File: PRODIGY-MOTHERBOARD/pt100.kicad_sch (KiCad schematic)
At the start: 5 parts, among them U10 LMP2011, U11 LMP2011, U17 LMP2011, U27 LMP2011, U9 LM4125AIM5-2.5

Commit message: Finished v0.1 schematic.
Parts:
- added C90: 100nF, symbol Device:C
- added C91: 47uF, symbol Device:C
- added JP10, JP9: Jumper_2_Open, symbol Jumper:Jumper_2_Open
- added R80: 2.5k, symbol Device:R
- added R81, R83, R84, R85, R86, R87: 10k, symbol Device:R
- added R82: 3.205k, symbol Device:R
- renumbered U10 to U23, U9 to U24, U11 to U25, U17 to U26
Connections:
- net at U26.1: now also R83.2, R85.1
- net GND: now reaches U26.2 (V-)
- net GND: now also U23.2 (V-), U24.2 (GND), U25.2 (V-), U27.2 (V-), C91.2, R80.2, R86.2
- net at U26.3 (+): now also R82.2, R83.1
- net RTD_W3: now reaches U26.4 (-)
- net RTD_W3: now also C90.2, JP10.1 (A)
- net +3.3VA: now reaches U26.5 (V+)
- net +3.3VA: now also U23.5 (V+), U24.4 (Vin), U25.5 (V+), U27.5 (V+)
- net RTD_A_OUT: now reaches U27.1
- net RTD_A_OUT: now also R87.2
- net at U27.3 (+): now also R84.2, R86.1
- net at U27.4 (-): now also R85.2, R87.1
- net at U24.5 (Vout): now also U23.3 (+), C91.1
- net RTD_W1: now reaches U23.1
- net RTD_W1: now also JP9.1 (A)
- net RTD_W4: now reaches U23.4 (-)
- net RTD_W4: now also JP10.2 (B), R80.1
- net at U25.1: now also R81.1, R84.1
- net RTD_W2: now reaches U25.3 (+)
- net RTD_W2: now also C90.1, JP9.2 (B)
- net at U25.4 (-): now also R81.2, R82.1
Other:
- note added: "2/3/4 Wire Configurator"
- note added: "Constant Current Source: 1mA 1mA = 2.5V / 2.5kOhm"
- note added: "Instrumentation Amplifier"
- note added: "Output voltage range: 0,1V - 0.34528V Gain: 2.5/0.34528 = 7.2405 R7 = 3.205k"
- moved on the sheet: U23, U24, U25, U26, U27

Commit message: schematic v0.2 finalized
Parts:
- renumbered C90 to C87, C91 to C88, JP9 to JP10, JP10 to JP11, R80 to R77, R81 to R78, R82 to R79, R83 to R80, R84 to R81, R85 to R82, R86 to R83, R87 to R84, U23 to U22, U24 to U23, U25 to U24, U26 to U25, U27 to U26

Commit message: Motherboard footprints assigned.
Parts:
- C87: footprint (none) -> Capacitor_SMD:C_0603_1608Metric
- C88: footprint (none) -> Capacitor_SMD:C_1210_3225Metric
- JP10, JP11: footprint (none) -> Connector_PinHeader_2.54mm:PinHeader_1x02_P2.54mm_Vertical
- R77, R78, R79, R80, R81, R82, R83, R84: footprint (none) -> Resistor_SMD:R_0603_1608Metric
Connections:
- net +3.3VA renamed VAA
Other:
- moved on the sheet: R79

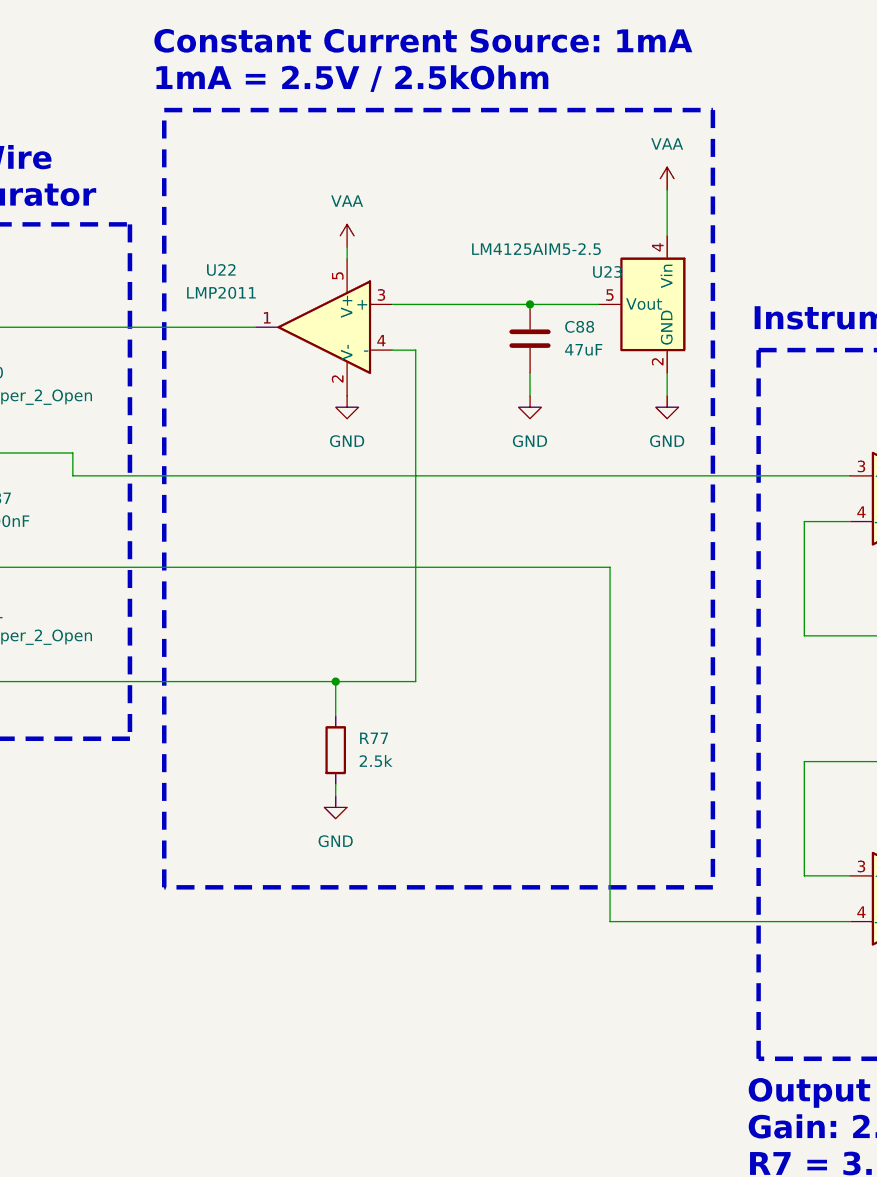
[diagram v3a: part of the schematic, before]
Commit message: finished motherboard bom and updated footprints
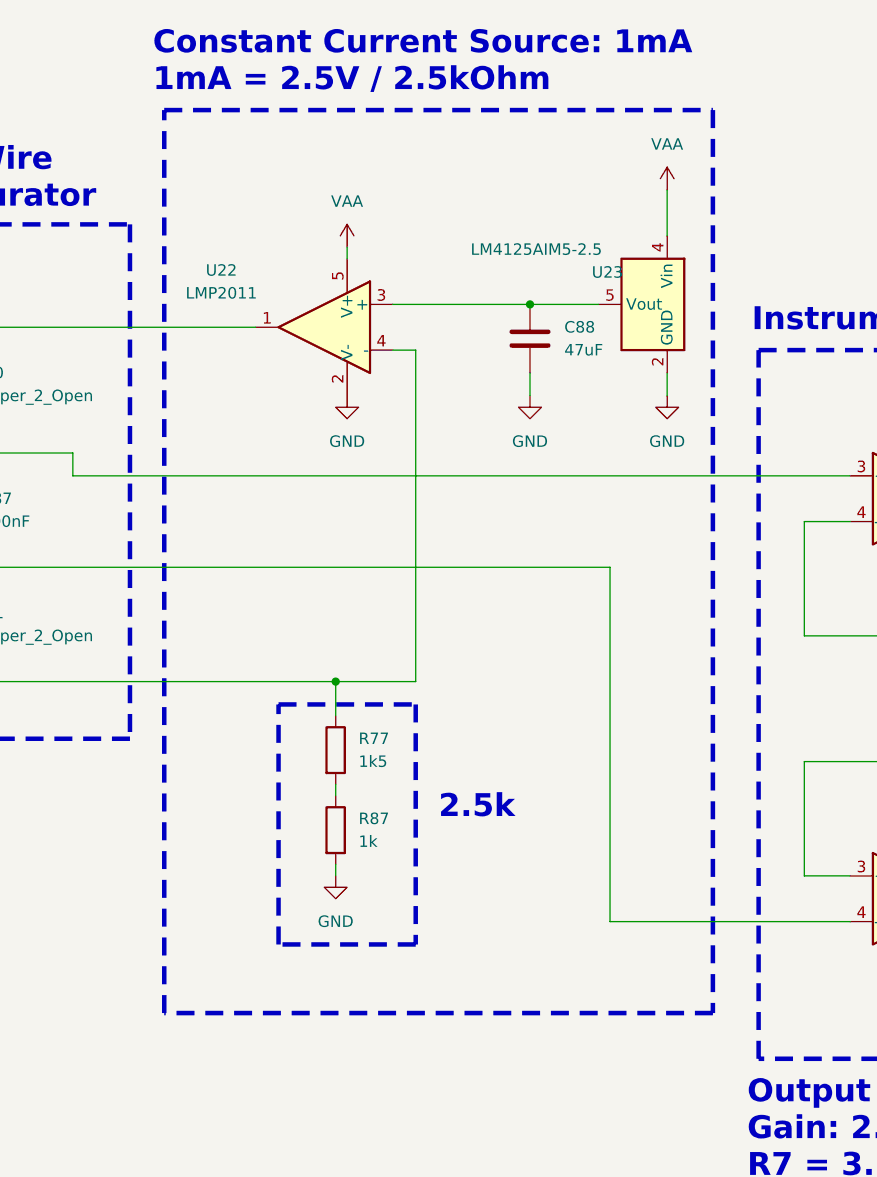
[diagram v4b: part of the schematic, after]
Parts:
- added R87: 1k, Resistor_SMD:R_0603_1608Metric, symbol Device:R
- C87: TME (none) -> CL10B104KB8NNNC
- C88: TME (none) -> GRM32ER61C476KE15L
- JP10, JP11: TME (none) -> JUMPER-H/B
- R77: value 2.5k -> 1k5; TME (none) -> WR06X1501FTL
- R78, R80, R81, R82, R83, R84: TME (none) -> WR06X1002FTL
- R79: TME (none) -> ERA3AEB332V
- U22, U24, U25, U26: MOUSER (none) -> 926-LMP2011MFX/NOPB
- U23: MOUSER (none) -> 926-LM4125IM525NOPB
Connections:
- net GND: now also R87.2; no longer R77.2
- new net: R77.2, R87.1
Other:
- note added: "2.5k"
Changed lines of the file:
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@@
 	(wire
 		(pts
-			(xy 114.3 114.3) (xy 114.3 113.03)
-		)
-		(stroke
-			(width 0)
-			(type default)
-		)
-	)
-	(wire
-		(pts
 			(xy 166.37 123.19) (xy 166.37 110.49)
 		)
@@
 	(wire
 		(pts
+			(xy 114.3 123.19) (xy 114.3 121.92)
+		)
+		(stroke
+			(width 0)
+			(type default)
+		)
+	)
+	(wire
+		(pts
 			(xy 199.39 96.52) (xy 199.39 99.06)
 		)
@@
 	(wire
 		(pts
+			(xy 114.3 113.03) (xy 114.3 114.3)
+		)
+		(stroke
+			(width 0)
+			(type default)
+		)
+	)
+	(wire
+		(pts
 			(xy 218.44 104.14) (xy 215.9 104.14)
 		)
@@
 	(rectangle
 		(start 95.25 38.1)
-		(end 156.21 124.46)
+		(end 156.21 138.43)
+		(stroke
+			(width 0.5)
+			(type dash)
+		)
+		(fill
+			(type none)
+		)
+	)
+	(rectangle
+		(start 107.95 104.14)
+		(end 123.19 130.81)
 		(stroke
 			(width 0.5)
@@
 		)
 	)
+	(text "2.5k"
+		(exclude_from_sim no)
+		(at 125.73 117.094 0)
+		(effects
+			(font
+				(size 2.54 2.54)
+				(thickness 0.508)
+				(bold yes)
+			)
+			(justify left bottom)
+		)
+	)
 	(hierarchical_label "RTD_W1"
 		(shape input)
@@
 			)
 		)
-		(property "MOUSER" ""
+		(property "MOUSER" " 926-LMP2011MFX/NOPB "
 			(at 179.07 125.73 0)
 			(effects
@@
 			)
 		)
-		(property "TME" ""
+		(property "TME" "WR06X1002FTL "
 			(at 199.39 120.65 0)
 			(effects
@@
 			)
 		)
-		(property "TME" ""
+		(property "TME" "GRM32ER61C476KE15L"
 			(at 135.89 63.5 0)
 			(effects
@@
 			)
 		)
-		(property "TME" ""
+		(property "TME" "JUMPER-H/B"
 			(at 71.12 68.58 0)
 			(effects
@@
 			)
 		)
-		(property "TME" ""
+		(property "TME" "WR06X1002FTL "
 			(at 209.55 81.28 0)
 			(effects
@@
 			)
 		)
-		(property "MOUSER" ""
+		(property "MOUSER" " 926-LMP2011MFX/NOPB "
 			(at 226.06 101.6 0)
 			(effects
@@
 			)
 		)
-		(property "TME" ""
+		(property "TME" "WR06X1002FTL "
 			(at 210.82 125.73 0)
 			(effects
@@
 			)
 		)
-		(property "TME" ""
+		(property "TME" "JUMPER-H/B"
 			(at 71.12 95.25 0)
 			(effects
@@
 			)
 		)
-		(property "MOUSER" ""
+		(property "MOUSER" " 926-LM4125IM525NOPB "
 			(at 151.13 59.69 0)
 			(effects
@@
 			)
 		)
-		(property "MOUSER" ""
+		(property "MOUSER" " 926-LMP2011MFX/NOPB "
 			(at 113.03 62.23 0)
 			(effects
@@
 			)
 		)
-		(property "TME" ""
+		(property "TME" "WR06X1002FTL "
 			(at 224.79 125.73 0)
 			(effects
@@
 			)
 		)
-		(property "TME" ""
+		(property "TME" "CL10B104KB8NNNC  "
 			(at 71.12 82.55 0)
 			(effects
@@
 	)
 	(symbol
+		(lib_id "Device:R")
+		(at 114.3 118.11 0)
+		(unit 1)
+		(exclude_from_sim no)
+		(in_bom yes)
+		(on_board yes)
+		(dnp no)
+		(property "Reference" "R87"
+			(at 116.84 116.8399 0)
+			(effects
+				(font
+					(size 1.27 1.27)
+				)
+				(justify left)
+			)
+		)
+		(property "Value" "1k"
+			(at 116.84 119.3799 0)
+			(effects
+				(font
+					(size 1.27 1.27)
+				)
+				(justify left)
+			)
+		)
+		(property "Footprint" "Resistor_SMD:R_0603_1608Metric"
+			(at 112.522 118.11 90)
+			(effects
+				(font
+					(size 1.27 1.27)
+				)
+				(hide yes)
+			)
+		)
+		(property "Datasheet" "~"
+			(at 114.3 118.11 0)
+			(effects
+				(font
+					(size 1.27 1.27)
+				)
+				(hide yes)
+			)
+		)
+		(property "Description" "Resistor"
+			(at 114.3 118.11 0)
+			(effects
+				(font
+					(size 1.27 1.27)
+				)
+				(hide yes)
+			)
+		)
+		(property "MOUSER" ""
+			(at 114.3 118.11 0)
+			(effects
+				(font
+					(size 1.27 1.27)
+				)
+				(hide yes)
+			)
+		)
+		(property "Sim.Type" ""
+			(at 114.3 118.11 0)
+			(effects
+				(font
+					(size 1.27 1.27)
+				)
+				(hide yes)
+			)
+		)
+		(property "TME" "RC0603JR-071K "
+			(at 114.3 118.11 0)
+			(effects
+				(font
+					(size 1.27 1.27)
+				)
+				(hide yes)
+			)
+		)
+		(pin "2"
+		)
+		(pin "1"
+		)
+		(instances
+			(project "PRODIGY-MOTHERBOARD"
+				(path "/f1c25860-8989-4190-bd24-2491d23ca7d9/1fb3a40b-5b56-4526-bac8-0d25e381d4b7"
+					(reference "R87")
+					(unit 1)
+				)
+			)
+		)
+	)
+	(symbol
 		(lib_id "power:VAA")
 		(at 176.53 72.39 0)
@@
 			)
 		)
-		(property "MOUSER" ""
+		(property "MOUSER" " 926-LMP2011MFX/NOPB "
 			(at 179.07 81.28 0)
 			(effects
@@
 			)
 		)
-		(property "Value" "2.5k"
+		(property "Value" "1k5"
 			(at 116.84 110.4899 0)
 			(effects
@@
 			)
 		)
-		(property "TME" ""
+		(property "TME" "WR06X1501FTL "
 			(at 114.3 109.22 0)
 			(effects
@@
 			)
 		)
-		(property "TME" ""
+		(property "TME" "ERA3AEB332V"
 			(at 199.39 102.87 0)
 			(effects
@@
 			)
 		)
-		(property "TME" ""
+		(property "TME" "WR06X1002FTL "
 			(at 199.39 86.36 0)
 			(effects
@@
 			)
 		)
-		(property "TME" ""
+		(property "TME" "WR06X1002FTL "
 			(at 223.52 81.28 0)
 			(effects
@@
 	(symbol
 		(lib_id "power:GND")
-		(at 114.3 114.3 0)
+		(at 114.3 123.19 0)
 		(unit 1)
 		(exclude_from_sim no)
@@
 		(fields_autoplaced yes)
 		(property "Reference" "#PWR0235"
-			(at 114.3 120.65 0)
+			(at 114.3 129.54 0)
 			(effects
 				(font
@@
 		)
 		(property "Value" "GND"
-			(at 114.3 119.38 0)
+			(at 114.3 128.27 0)
 			(effects
 				(font
@@
 		)
 		(property "Footprint" ""
-			(at 114.3 114.3 0)
+			(at 114.3 123.19 0)
 			(effects
 				(font
@@
 		)
 		(property "Datasheet" ""
-			(at 114.3 114.3 0)
+			(at 114.3 123.19 0)
 			(effects
 				(font
@@
 		)
 		(property "Description" "Power symbol creates a global label with name \"GND\" , ground"
-			(at 114.3 114.3 0)
+			(at 114.3 123.19 0)
 			(effects
 				(font
